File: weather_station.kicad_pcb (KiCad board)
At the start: 2 copper layers, 100 x 140 mm, 115 parts, among them J2 Conn_02x10_Odd_Even, J3 Conn_Coaxial, J4 Conn_Coaxial, J5 THERM, J6 SOLAR, M1 ANEOMETER, Q1 Q_NMOS_DGS, Q2 FDMS8050, Q3 FDMS8050, Q4 FDMS8050, Q5 FDMS8050, U1 LT1129CS8-3.3, U2 ADS1120-PW, U3 nRF52832, U4 BQ24650, U5 MPL115A1, U6 MPU-9250, Y1 FL3200037, Y2 32.786khz

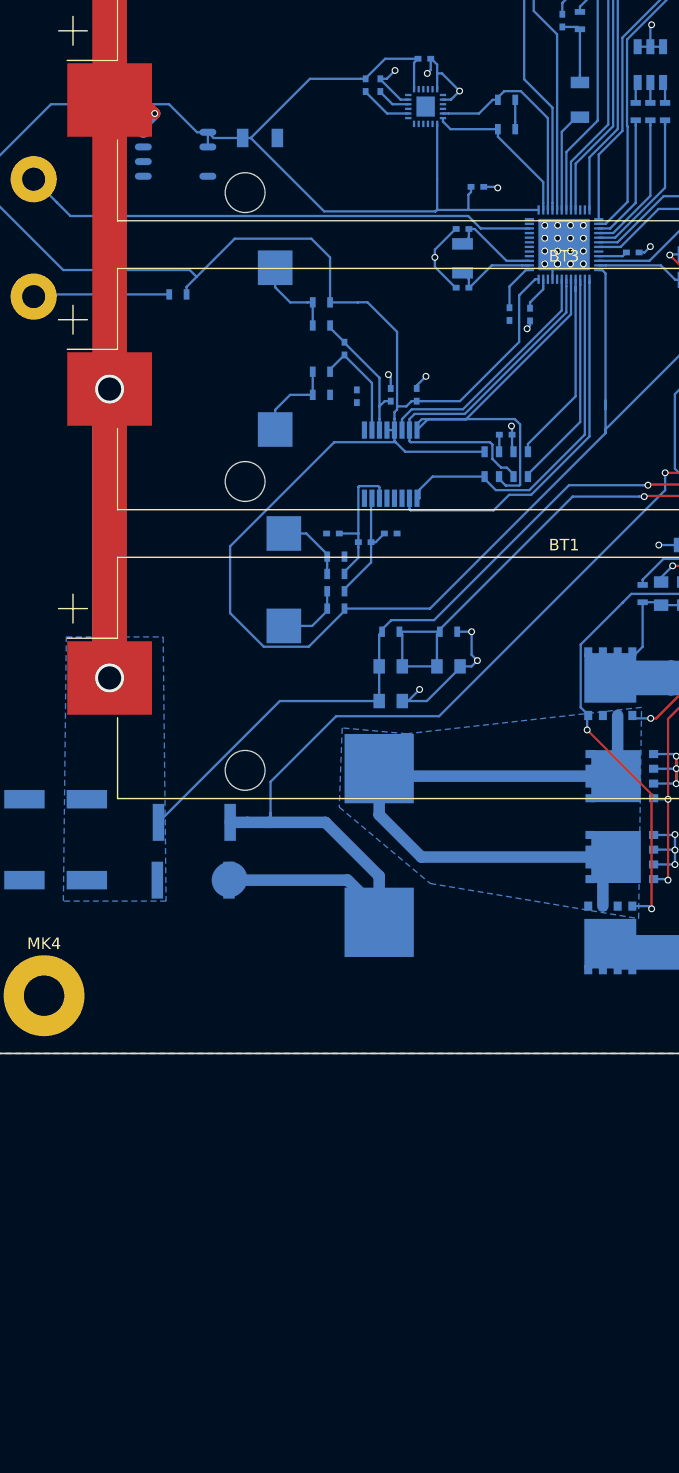
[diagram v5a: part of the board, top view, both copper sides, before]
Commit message: might as well be able to monitor battery voltage from the nrf52832
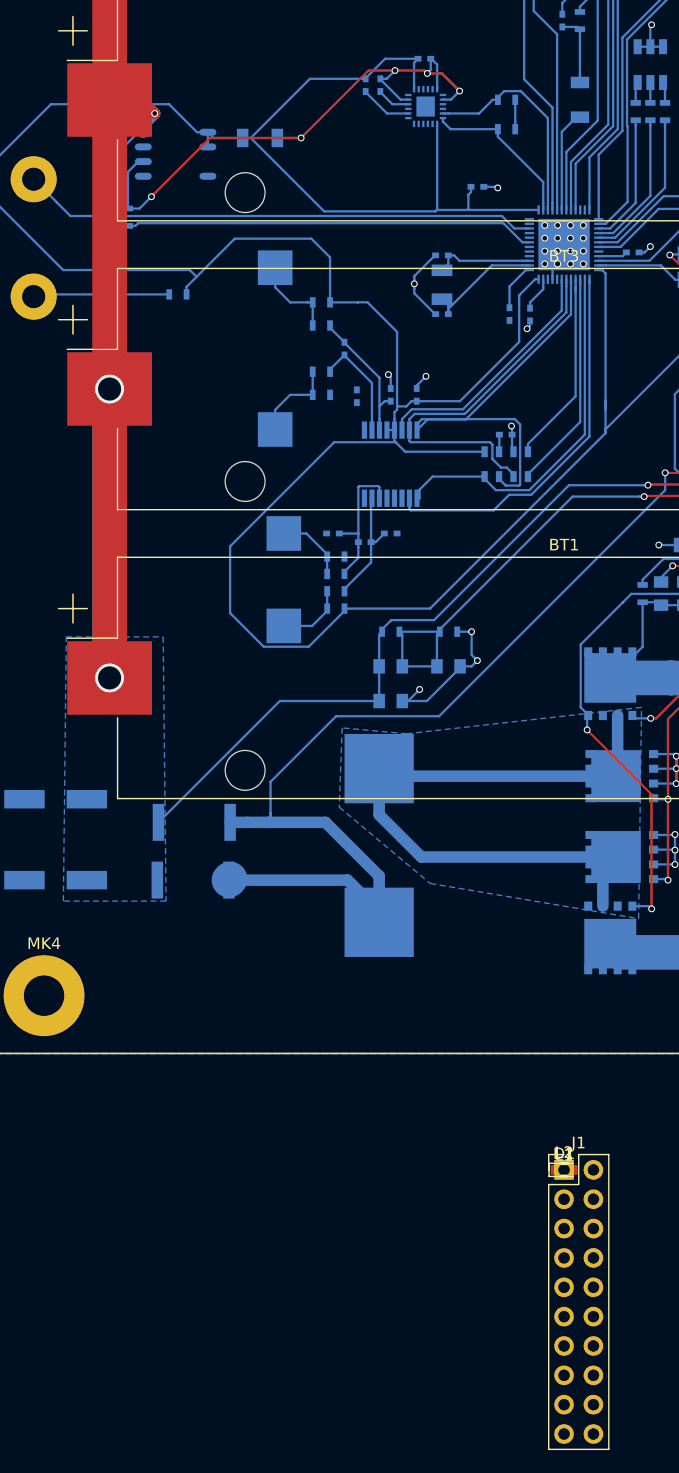
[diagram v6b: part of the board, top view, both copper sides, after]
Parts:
- added D1: D_Zener, Diodes_SMD:D_0603, F.Cu at (70.0, 170.1)
- added J1: Conn_02x10_Odd_Even, Pin_Headers:Pin_Header_Straight_2x10_Pitch2.54mm, F.Cu at (70.0, 170.1)
- added L1: 15uH, Capacitors_SMD:C_0402, F.Cu at (70.0, 170.1)
- added L2: 10uH, Capacitors_SMD:C_0603, F.Cu at (70.0, 170.1)
- added R31: R_Small, Resistors_SMD:R_0603, B.Cu at (30.5, 87.6)
- added R32: R_Small, Resistors_SMD:R_0603, B.Cu at (32.3, 87.6)
- moved C29 2.90 mm to (59.4, 90.9)
- moved C30 2.90 mm to (59.4, 96.0)
- moved Y2 2.90 mm to (59.4, 93.5)
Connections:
- U3 pad 7: Net-(U3-Pad7) -> v_batt
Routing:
- net GND: track 157.2 -> 198.5 mm, vias 59 -> 61
- net v_batt: track 0.00 -> 37.3 mm
- net VCC: track 236.3 -> 244.5 mm
- net XL1: track 7.55 -> 10.6 mm
- net XL2: track 7.89 -> 8.73 mm

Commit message: i think that's enough for now
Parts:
- removed D1: D_Zener, Diodes_SMD:D_0603
- removed J1: Conn_02x10_Odd_Even, Pin_Headers:Pin_Header_Straight_2x10_Pitch2.54mm
- removed J5: THERM, Connectors_Terminal_Blocks:TerminalBlock_Pheonix_MPT-2.54mm_2pol
- removed L1: 15uH, Capacitors_SMD:C_0402
- removed L2: 10uH, Capacitors_SMD:C_0603
- added TH1: Thermistor_NTC, Resistors_SMD:R_0805, F.Cu at (101.9, 89.9)
- C12, C13: value C_Small -> tuning_cap
- C35, C43: value CP -> 100uF
- C36, C40: value CP -> 47uF
- L4: value L_Small -> tuning_inductor
- R14: value 10k -> 10kΩ
- R15, R25, R26: value 5.23k -> 5.23kΩ
- R16: value 100K -> 100kΩ
- R17: value 3.3k -> 3.3kΩ
- R18: value 1.8K -> 1.8KΩ
- R19: value 30.1k -> 30.1kΩ
- R20, R29: value 499k -> 499kΩ
- R21: value R_Small -> 100kΩ
- R22: value 36k -> 36kΩ
- R24: value 10 -> 10Ω
- R27, R28: value 0.010 -> 0.010Ω
- R30: value 100k -> 100kΩ
- R31: value R_Small -> 1MΩ
- R32: value R_Small -> 499kΩ
- moved C19 14.0 mm to (101.8, 93.5), turned to 0 degrees
- moved C28 13.3 mm to (101.8, 95.5), turned to 0 degrees
- moved R15 13.2 mm to (101.8, 97.4), turned to 180 degrees
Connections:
- BT1 pad 1: VCC -> +BATT
- BT2 pad 1: VCC -> +BATT
- BT3 pad 1: VCC -> +BATT
- BT4 pad 1: VCC -> +BATT
- C2 pad 2: VCC -> +BATT
- C38 pad 1: VCC -> +BATT
- C39 pad 1: VCC -> +BATT
- C40 pad 1: VCC -> +BATT
- C41 pad 2: VCC -> +BATT
- C43 pad 1: VCC -> +BATT
- DRA1 pad 8: VCC -> +BATT
- R27 pad 2: VCC -> +BATT
- R28 pad 1: VCC -> +BATT
- R29 pad 1: VCC -> +BATT
- R31 pad 1: VCC -> +BATT
- U1 pad 8: VCC -> +BATT
- U4 pad 9: VCC -> +BATT
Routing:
- net GND: track 198.5 -> 518.6 mm, vias 61 -> 66
- net +BATT: track 0.00 -> 258.2 mm, vias 0 -> 7
- net VCC: track 244.5 -> 0.00 mm, vias 7 -> 0
- net Net-(C19-Pad1): track 62.9 -> 41.9 mm, vias 2 -> 3
- net /power/VREF: track 46.0 -> 37.4 mm
- net SDA: track 13.9 -> 21.7 mm
- net +3V3: track 321.6 -> 328.0 mm
- net (no net): track 0.00 -> 6.00 mm
- net SCL: track 18.9 -> 20.9 mm
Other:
- board text added: "KN4GRT"

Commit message: 139
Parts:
- R31: value 1MΩ -> 100kΩ
- R32: value 499kΩ -> 100kΩ
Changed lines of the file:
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@@
       (effects (font (size 1 1) (thickness 0.15)) (justify mirror))
     )
-    (fp_text value 1MΩ (at 0 -1.5 270) (layer B.Fab)
+    (fp_text value 100kΩ (at 0 -1.5 270) (layer B.Fab)
       (effects (font (size 1 1) (thickness 0.15)) (justify mirror))
     )
@@
       (effects (font (size 1 1) (thickness 0.15)) (justify mirror))
     )
-    (fp_text value 499kΩ (at 0 -1.5 90) (layer B.Fab)
+    (fp_text value 100kΩ (at 0 -1.5 90) (layer B.Fab)
       (effects (font (size 1 1) (thickness 0.15)) (justify mirror))
     )
